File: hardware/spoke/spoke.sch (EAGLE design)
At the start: 23 parts, among them IC1 7805TV, IC2 LM3490, J1 AVR_SPI_PRG_6PTH, J2 POWER_JACKPTH, U1 ATMEGA328P_PDIP, U3 NRF24L01+

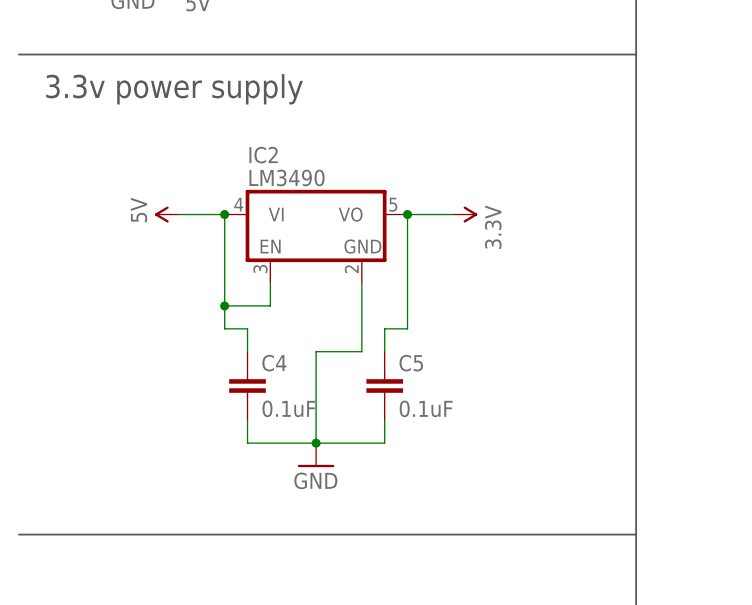
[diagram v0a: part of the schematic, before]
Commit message: Move from LM3490 to LM3940 regulator
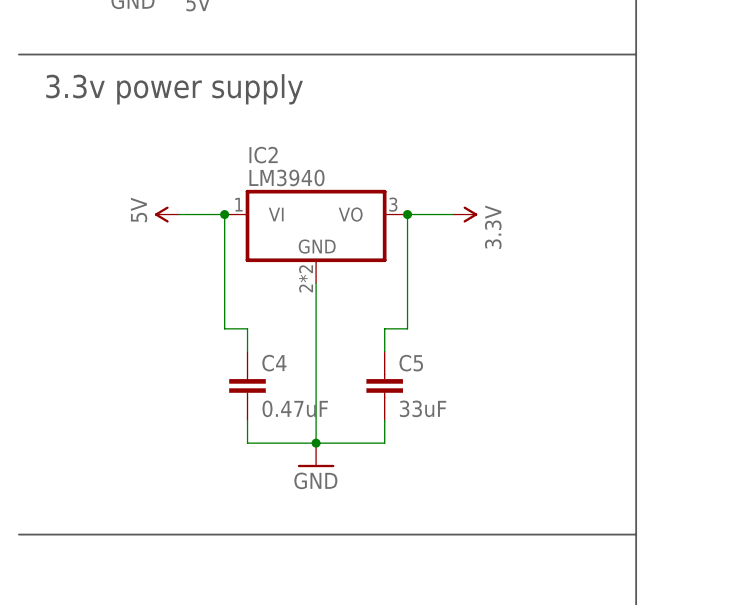
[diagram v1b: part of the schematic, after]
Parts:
- C4: value 0.1uF -> 0.47uF
- C5: value 0.1uF -> 33uF
- IC2: value LM3490 -> LM3940; device aurai:LM3490 -> aurai:LM3940
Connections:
- net 5V: no longer IC2.ENABLE
- net GND: now also IC2.GND; no longer IC2.GND1
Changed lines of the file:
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@@
 <part name="SUPPLY9" library="SparkFun-Aesthetics" deviceset="5V" device=""/>
 <part name="GND6" library="SparkFun-Aesthetics" deviceset="GND" device=""/>
-<part name="C4" library="SparkFun-Capacitors" deviceset="CAP" device="0805" value="0.1uF"/>
-<part name="C5" library="SparkFun-Capacitors" deviceset="CAP" device="0805" value="0.1uF"/>
-<part name="IC2" library="aurai" deviceset="LM3490" device=""/>
+<part name="C4" library="SparkFun-Capacitors" deviceset="CAP" device="0805" value="0.47uF"/>
+<part name="C5" library="SparkFun-Capacitors" deviceset="CAP" device="0805" value="33uF"/>
 <part name="R1" library="aurai" deviceset="CRA06ES08" device="" value="330"/>
+<part name="IC2" library="aurai" deviceset="LM3940" device=""/>
 </parts>
 <sheets>
@@
 <instance part="C4" gate="G$1" x="25.4" y="60.96"/>
 <instance part="C5" gate="G$1" x="40.64" y="60.96"/>
+<instance part="R1" gate="R" x="190.5" y="116.84" rot="MR0"/>
 <instance part="IC2" gate="IC" x="33.02" y="81.28"/>
-<instance part="R1" gate="R" x="190.5" y="116.84" rot="MR0"/>
 </instances>
 <busses>
@@
 <segment>
 <pinref part="GND6" gate="1" pin="GND"/>
-<wire x1="33.02" y1="66.04" x2="33.02" y2="55.88" width="0.1524" layer="91"/>
+<wire x1="33.02" y1="73.66" x2="33.02" y2="55.88" width="0.1524" layer="91"/>
 <wire x1="40.64" y1="55.88" x2="33.02" y2="55.88" width="0.1524" layer="91"/>
 <junction x="33.02" y="55.88"/>
@@
 <pinref part="C4" gate="G$1" pin="2"/>
 <pinref part="C5" gate="G$1" pin="2"/>
-<pinref part="IC2" gate="IC" pin="GND1"/>
-<wire x1="38.1" y1="73.66" x2="38.1" y2="66.04" width="0.1524" layer="91"/>
-<wire x1="38.1" y1="66.04" x2="33.02" y2="66.04" width="0.1524" layer="91"/>
+<pinref part="IC2" gate="IC" pin="GND"/>
 </segment>
 </net>
@@
 <wire x1="25.4" y1="66.04" x2="25.4" y2="68.58" width="0.1524" layer="91"/>
 <wire x1="25.4" y1="68.58" x2="22.86" y2="68.58" width="0.1524" layer="91"/>
+<pinref part="SUPPLY7" gate="G$1" pin="5V"/>
+<wire x1="22.86" y1="68.58" x2="22.86" y2="81.28" width="0.1524" layer="91"/>
+<wire x1="22.86" y1="81.28" x2="17.78" y2="81.28" width="0.1524" layer="91"/>
 <pinref part="IC2" gate="IC" pin="VI"/>
-<pinref part="SUPPLY7" gate="G$1" pin="5V"/>
 <junction x="22.86" y="81.28"/>
-<wire x1="22.86" y1="68.58" x2="22.86" y2="71.12" width="0.1524" layer="91"/>
-<wire x1="22.86" y1="71.12" x2="22.86" y2="81.28" width="0.1524" layer="91"/>
-<wire x1="22.86" y1="81.28" x2="17.78" y2="81.28" width="0.1524" layer="91"/>
-<pinref part="IC2" gate="IC" pin="ENABLE"/>
-<wire x1="27.94" y1="73.66" x2="27.94" y2="71.12" width="0.1524" layer="91"/>
-<wire x1="27.94" y1="71.12" x2="22.86" y2="71.12" width="0.1524" layer="91"/>
-<junction x="22.86" y="71.12"/>
-</segment>
-</net>
+</segment>
+</net>
